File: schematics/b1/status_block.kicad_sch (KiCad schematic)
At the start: 23 parts, among them Q1 2N3904, SW5 SW_SPDT, U4 74HC595

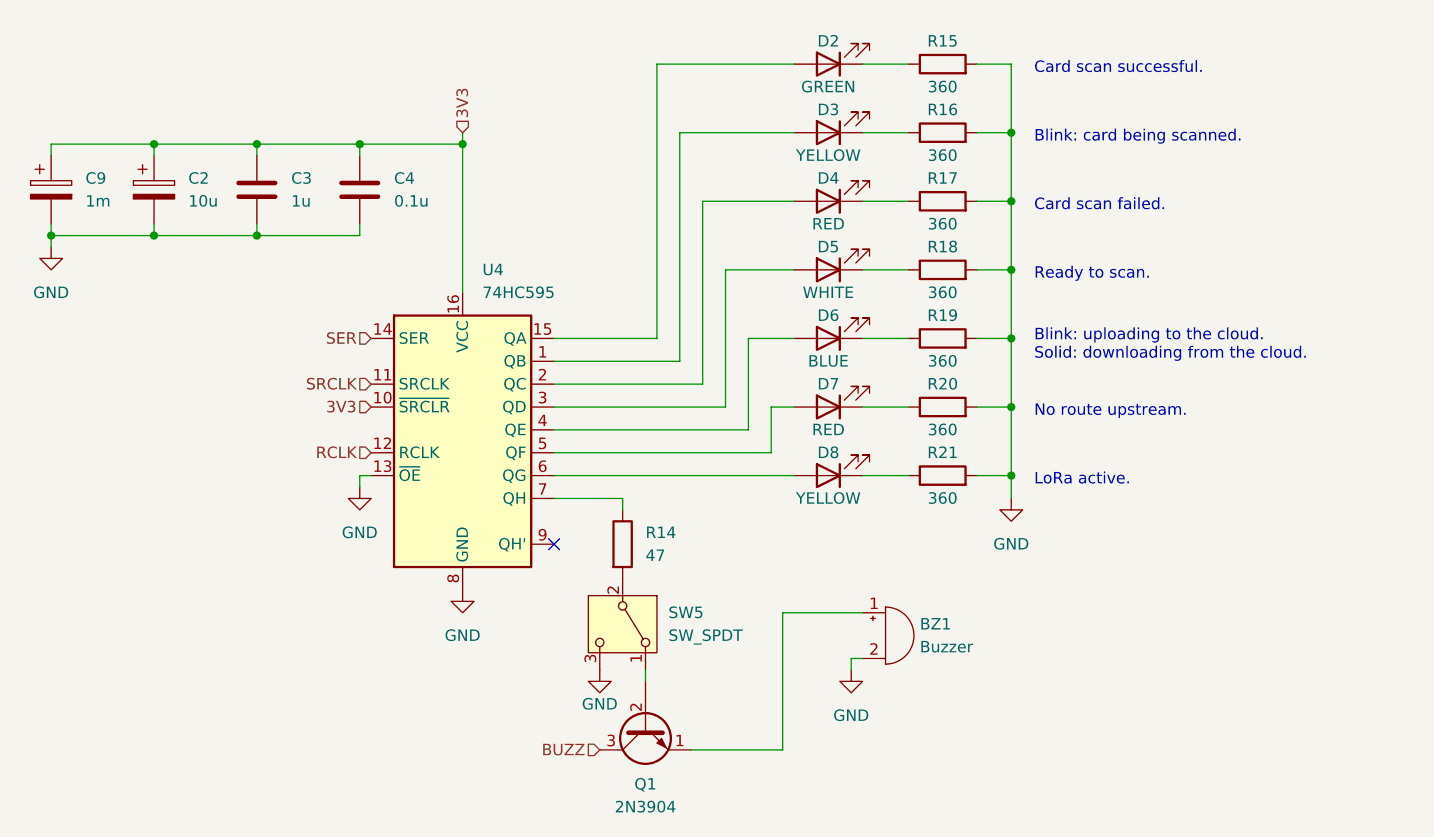
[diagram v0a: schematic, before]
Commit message: Added a bunch of test points.
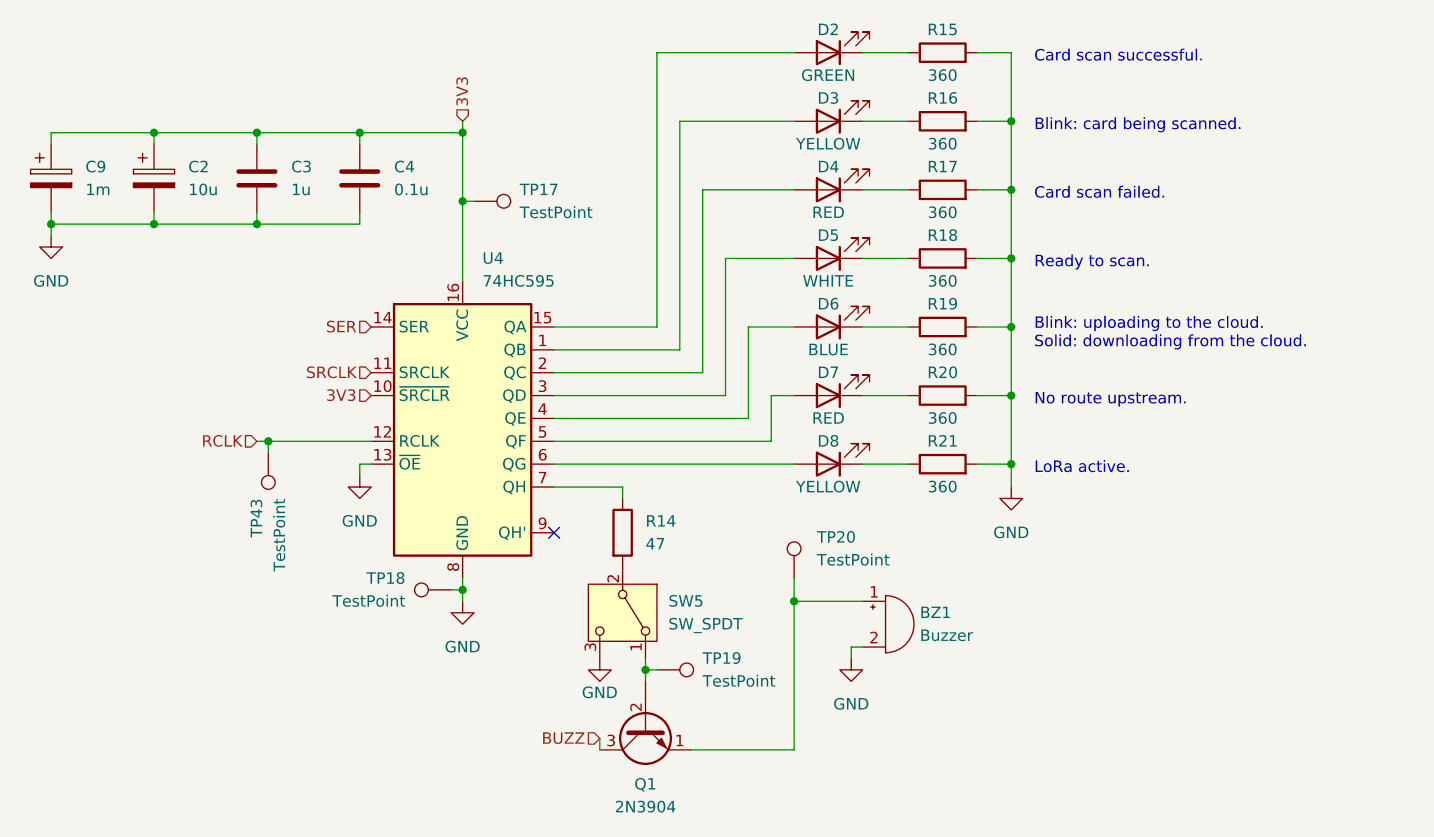
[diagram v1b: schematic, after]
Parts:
- added TP17, TP18, TP19, TP20, TP43: TestPoint, symbol Connector:TestPoint
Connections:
- net 3V3: now also TP17.1
- net GND: now also TP18.1
- net RCLK: now also TP43.1
- net at BZ1.1 (+), Q1.1 (E): now also TP20.1
- net at Q1.2 (B), SW5.1 (A): now also TP19.1
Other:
- moved on the sheet: BZ1, C2, C3, C4, C9, D2, D3, D4, D5, D6, D7, D8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

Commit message: Updated annotations.
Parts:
- renumbered C9 to C21, C2 to C22, C3 to C23, C4 to C24, D2 to D1, D3 to D2, D4 to D3, D5 to D4, D6 to D5, D7 to D6, D8 to D7, R15 to R14, R16 to R15, R17 to R16, R18 to R17, R19 to R18, R20 to R19, R21 to R20, R14 to R21, SW5 to SW6, TP17 to TP32, TP43 to TP33, TP20 to TP34, TP18 to TP35, TP19 to TP36, U4 to U6

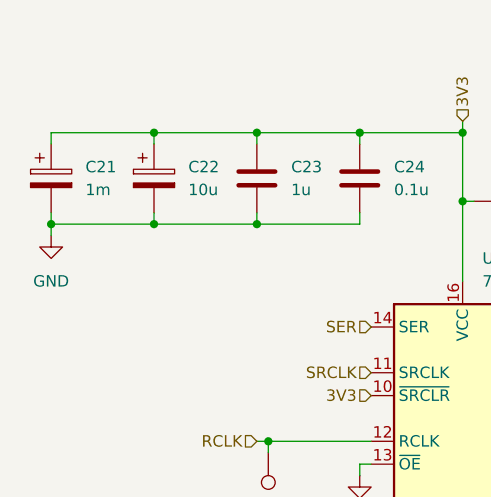
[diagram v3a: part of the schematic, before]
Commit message: Tweaked wiring.
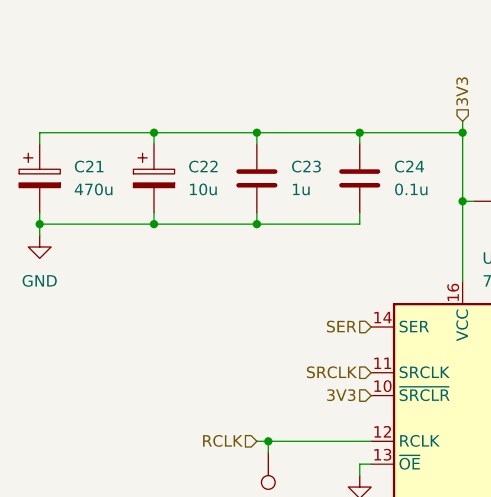
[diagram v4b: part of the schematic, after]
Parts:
- C21: value 1m -> 470u
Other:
- moved on the sheet: C21
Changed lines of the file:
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@@
   (junction (at 45.72 36.83) (diameter 0) (color 0 0 0 0)
   )
-  (junction (at 34.29 36.83) (diameter 0) (color 0 0 0 0)
+  (junction (at 33.02 36.83) (diameter 0) (color 0 0 0 0)
   )
   (junction (at 57.15 26.67) (diameter 0) (color 0 0 0 0)
@@
   )
   (no_connect (at 90.17 71.12))
-  (wire (pts (xy 34.29 27.94) (xy 34.29 26.67))
+  (wire (pts (xy 33.02 27.94) (xy 33.02 26.67))
     (stroke (width 0) (type default))
   )
@@
     (stroke (width 0) (type default))
   )
-  (wire (pts (xy 34.29 38.1) (xy 34.29 36.83))
+  (wire (pts (xy 33.02 38.1) (xy 33.02 36.83))
     (stroke (width 0) (type default))
   )
@@
     (stroke (width 0) (type default))
   )
-  (wire (pts (xy 34.29 35.56) (xy 34.29 36.83))
+  (wire (pts (xy 33.02 35.56) (xy 33.02 36.83))
     (stroke (width 0) (type default))
   )
@@
     (stroke (width 0) (type default))
   )
-  (wire (pts (xy 34.29 36.83) (xy 45.72 36.83))
+  (wire (pts (xy 33.02 36.83) (xy 45.72 36.83))
     (stroke (width 0) (type default))
   )
@@
     (stroke (width 0) (type default))
   )
-  (wire (pts (xy 34.29 26.67) (xy 45.72 26.67))
+  (wire (pts (xy 33.02 26.67) (xy 45.72 26.67))
     (stroke (width 0) (type default))
   )
@@
     )
   )
-  (symbol (lib_id "power:GND") (at 34.29 38.1 0) (unit 1)
+  (symbol (lib_id "power:GND") (at 33.02 38.1 0) (unit 1)
     (in_bom yes) (on_board yes) (dnp no) (fields_autoplaced)
-    (property "Reference" "#PWR029" (at 34.29 44.45 0)
-      (effects (font (size 1.27 1.27)) hide)
-    )
-    (property "Value" "GND" (at 34.29 43.18 0)
-      (effects (font (size 1.27 1.27)))
-    )
-    (property "Footprint" "" (at 34.29 38.1 0)
-      (effects (font (size 1.27 1.27)) hide)
-    )
-    (property "Datasheet" "" (at 34.29 38.1 0)
+    (property "Reference" "#PWR029" (at 33.02 44.45 0)
+      (effects (font (size 1.27 1.27)) hide)
+    )
+    (property "Value" "GND" (at 33.02 43.18 0)
+      (effects (font (size 1.27 1.27)))
+    )
+    (property "Footprint" "" (at 33.02 38.1 0)
+      (effects (font (size 1.27 1.27)) hide)
+    )
+    (property "Datasheet" "" (at 33.02 38.1 0)
       (effects (font (size 1.27 1.27)) hide)
     )
@@
     )
   )
-  (symbol (lib_id "Device:C_Polarized") (at 34.29 31.75 0) (unit 1)
-    (in_bom yes) (on_board yes) (dnp no)
-    (property "Reference" "C21" (at 38.1 30.48 0)
-      (effects (font (size 1.27 1.27)) (justify left))
-    )
-    (property "Value" "1m" (at 38.1 33.02 0)
-      (effects (font (size 1.27 1.27)) (justify left))
-    )
-    (property "Footprint" "" (at 35.2552 35.56 0)
-      (effects (font (size 1.27 1.27)) hide)
-    )
-    (property "Datasheet" "~" (at 34.29 31.75 0)
-      (effects (font (size 1.27 1.27)) hide)
-    )
+  (symbol (lib_id "Device:C_Polarized") (at 33.02 31.75 0) (unit 1)
+    (in_bom yes) (on_board yes) (dnp no)
+    (property "Reference" "C21" (at 36.83 30.48 0)
+      (effects (font (size 1.27 1.27)) (justify left))
+    )
+    (property "Value" "470u" (at 36.83 33.02 0)
+      (effects (font (size 1.27 1.27)) (justify left))
+    )
+    (property "Footprint" "" (at 33.9852 35.56 0)
+      (effects (font (size 1.27 1.27)) hide)
+    )
+    (property "Datasheet" "~" (at 33.02 31.75 0)
+      (effects (font (size 1.27 1.27)) hide)
+    )

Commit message: Assigned some footprints.
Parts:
- BZ1: footprint (none) -> Buzzer_Beeper:Buzzer_12x9.5RM7.6
- C21: footprint (none) -> Capacitor_THT:CP_Radial_D8.0mm_P3.80mm
- C22: footprint (none) -> Capacitor_THT:CP_Radial_D4.0mm_P2.00mm
- C23, C24: footprint (none) -> Capacitor_SMD:C_1206_3216Metric_Pad1.33x1.80mm_HandSolder
- D1, D2, D3, D4, D5, D6, D7: footprint (none) -> LED_THT:LED_D5.0mm
- Q1: footprint Package_TO_SOT_THT:TO-92_Inline -> (none)
- R14, R15, R16, R17, R18, R19, R20, R21: footprint (none) -> Resistor_THT:R_Axial_DIN0207_L6.3mm_D2.5mm_P7.62mm_Horizontal
- SW6: footprint (none) -> custom:SW_SPDT
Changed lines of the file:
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@@
       (effects (font (size 1.27 1.27)))
     )
-    (property "Footprint" "" (at 133.35 27.178 90)
+    (property "Footprint" "Resistor_THT:R_Axial_DIN0207_L6.3mm_D2.5mm_P7.62mm_Horizontal" (at 133.35 27.178 90)
       (effects (font (size 1.27 1.27)) hide)
     )
@@
       (effects (font (size 1.27 1.27)))
     )
-    (property "Footprint" "" (at 120.65 63.5 0)
+    (property "Footprint" "LED_THT:LED_D5.0mm" (at 120.65 63.5 0)
       (effects (font (size 1.27 1.27)) hide)
     )
@@
       (effects (font (size 1.27 1.27)) (justify left))
     )
-    (property "Footprint" "" (at 58.1152 35.56 0)
+    (property "Footprint" "Capacitor_SMD:C_1206_3216Metric_Pad1.33x1.80mm_HandSolder" (at 58.1152 35.56 0)
       (effects (font (size 1.27 1.27)) hide)
     )
@@
       (effects (font (size 1.27 1.27)))
     )
-    (property "Footprint" "" (at 120.65 48.26 0)
+    (property "Footprint" "LED_THT:LED_D5.0mm" (at 120.65 48.26 0)
       (effects (font (size 1.27 1.27)) hide)
     )
@@
       (effects (font (size 1.27 1.27)))
     )
-    (property "Footprint" "" (at 133.35 19.558 90)
+    (property "Footprint" "Resistor_THT:R_Axial_DIN0207_L6.3mm_D2.5mm_P7.62mm_Horizontal" (at 133.35 19.558 90)
       (effects (font (size 1.27 1.27)) hide)
     )
@@
       (effects (font (size 1.27 1.27)) (justify left))
     )
-    (property "Footprint" "" (at 46.6852 35.56 0)
+    (property "Footprint" "Capacitor_THT:CP_Radial_D4.0mm_P2.00mm" (at 46.6852 35.56 0)
       (effects (font (size 1.27 1.27)) hide)
     )
@@
       (effects (font (size 1.27 1.27)))
     )
-    (property "Footprint" "" (at 133.35 57.658 90)
+    (property "Footprint" "Resistor_THT:R_Axial_DIN0207_L6.3mm_D2.5mm_P7.62mm_Horizontal" (at 133.35 57.658 90)
       (effects (font (size 1.27 1.27)) hide)
     )
@@
       (effects (font (size 1.27 1.27)) (justify left))
     )
-    (property "Footprint" "" (at 33.9852 35.56 0)
+    (property "Footprint" "Capacitor_THT:CP_Radial_D8.0mm_P3.80mm" (at 33.9852 35.56 0)
       (effects (font (size 1.27 1.27)) hide)
     )
@@
       (effects (font (size 1.27 1.27)))
     )
-    (property "Footprint" "" (at 120.65 55.88 0)
+    (property "Footprint" "LED_THT:LED_D5.0mm" (at 120.65 55.88 0)
       (effects (font (size 1.27 1.27)) hide)
     )
@@
       (effects (font (size 1.27 1.27)))
     )
-    (property "Footprint" "Package_TO_SOT_THT:TO-92_Inline" (at 102.235 97.79 0)
+    (property "Footprint" "" (at 102.235 97.79 0)
       (effects (font (size 1.27 1.27) italic) (justify left) hide)
     )
@@
       (effects (font (size 1.27 1.27)))
     )
-    (property "Footprint" "" (at 120.65 25.4 0)
+    (property "Footprint" "LED_THT:LED_D5.0mm" (at 120.65 25.4 0)
       (effects (font (size 1.27 1.27)) hide)
     )
@@
       (effects (font (size 1.27 1.27)))
     )
-    (property "Footprint" "" (at 120.65 17.78 0)
+    (property "Footprint" "LED_THT:LED_D5.0mm" (at 120.65 17.78 0)
       (effects (font (size 1.27 1.27)) hide)
     )
@@
       (effects (font (size 1.27 1.27)))
     )
-    (property "Footprint" "" (at 133.35 34.798 90)
+    (property "Footprint" "Resistor_THT:R_Axial_DIN0207_L6.3mm_D2.5mm_P7.62mm_Horizontal" (at 133.35 34.798 90)
       (effects (font (size 1.27 1.27)) hide)
     )
@@
       (effects (font (size 1.27 1.27)))
     )
-    (property "Footprint" "" (at 120.65 40.64 0)
+    (property "Footprint" "LED_THT:LED_D5.0mm" (at 120.65 40.64 0)
       (effects (font (size 1.27 1.27)) hide)
     )
@@
       (effects (font (size 1.27 1.27)) (justify left))
     )
-    (property "Footprint" "" (at 126.365 78.74 90)
+    (property "Footprint" "Buzzer_Beeper:Buzzer_12x9.5RM7.6" (at 126.365 78.74 90)
       (effects (font (size 1.27 1.27)) hide)
     )
@@
       (effects (font (size 1.27 1.27)) (justify left))
     )
-    (property "Footprint" "" (at 69.5452 35.56 0)
+    (property "Footprint" "Capacitor_SMD:C_1206_3216Metric_Pad1.33x1.80mm_HandSolder" (at 69.5452 35.56 0)
       (effects (font (size 1.27 1.27)) hide)
     )
@@
       (effects (font (size 1.27 1.27)))
     )
-    (property "Footprint" "" (at 133.35 65.278 90)
+    (property "Footprint" "Resistor_THT:R_Axial_DIN0207_L6.3mm_D2.5mm_P7.62mm_Horizontal" (at 133.35 65.278 90)
       (effects (font (size 1.27 1.27)) hide)
     )
@@
       (effects (font (size 1.27 1.27)))
     )
-    (property "Footprint" "" (at 120.65 33.02 0)
+    (property "Footprint" "LED_THT:LED_D5.0mm" (at 120.65 33.02 0)
       (effects (font (size 1.27 1.27)) hide)
     )
@@
       (effects (font (size 1.27 1.27)))
     )
-    (property "Footprint" "" (at 133.35 50.038 90)
+    (property "Footprint" "Resistor_THT:R_Axial_DIN0207_L6.3mm_D2.5mm_P7.62mm_Horizontal" (at 133.35 50.038 90)
       (effects (font (size 1.27 1.27)) hide)
     )
@@
       (effects (font (size 1.27 1.27)) (justify left))
     )
-    (property "Footprint" "" (at 96.012 71.12 90)
+    (property "Footprint" "Resistor_THT:R_Axial_DIN0207_L6.3mm_D2.5mm_P7.62mm_Horizontal" (at 96.012 71.12 90)
       (effects (font (size 1.27 1.27)) hide)
     )
@@
       (effects (font (size 1.27 1.27)) (justify left))
     )
-    (property "Footprint" "" (at 97.79 80.01 0)
+    (property "Footprint" "custom:SW_SPDT" (at 97.79 80.01 0)
       (effects (font (size 1.27 1.27)) hide)
     )
@@
       (effects (font (size 1.27 1.27)))
     )
-    (property "Footprint" "" (at 133.35 42.418 90)
-      (effects (font (size 1.27 1.27)) hide)
-    )
+    (property "Footprint" "Resistor_THT:R_Axial_DIN0207_L6.3mm_D2.5mm_P7.62mm_Horizontal" (at 133.35 42.418 90)
+      (effects (font (size 1.27 1.27)) hide)
+    )

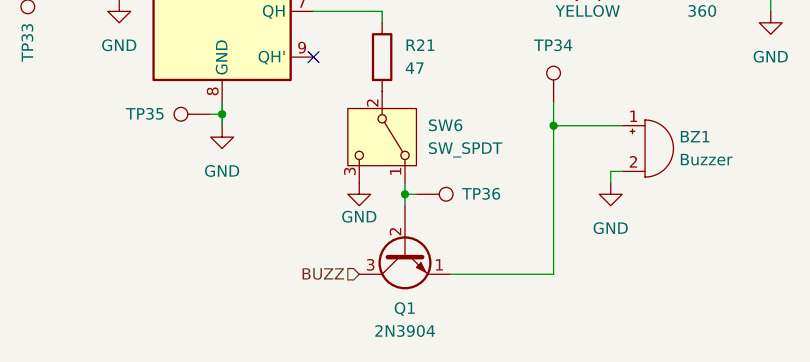
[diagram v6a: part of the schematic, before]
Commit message: Finished assigning footprints.
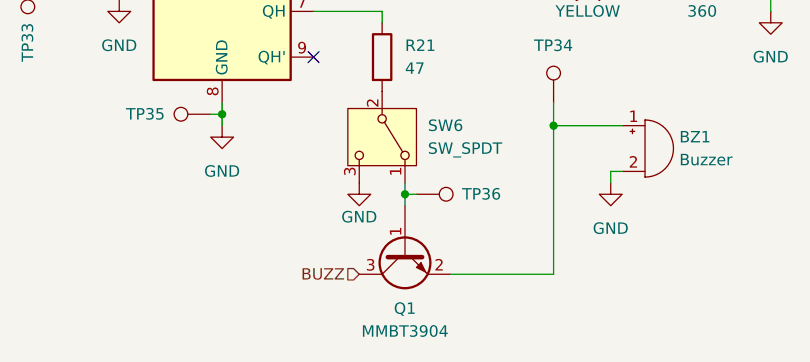
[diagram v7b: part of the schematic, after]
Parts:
- Q1: value 2N3904 -> MMBT3904; footprint (none) -> Package_TO_SOT_SMD:SOT-23; symbol Transistor_BJT:2N3904 -> Transistor_BJT:MMBT3904
- TP32, TP33, TP34, TP35, TP36: footprint (none) -> TestPoint:TestPoint_Loop_D2.50mm_Drill1.0mm
- U6: footprint (none) -> SN74HC595N:DIP794W45P254L1969H508Q16
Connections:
- net at BZ1.1 (+), TP34.1: now also Q1.2 (E); no longer Q1.1 (E)
- net at SW6.1 (A), TP36.1: now also Q1.1 (B); no longer Q1.2 (B)
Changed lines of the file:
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@@
       (effects (font (size 1.27 1.27)) (justify left) hide)
     )
-    (property "Footprint" "" (at 53.34 62.23 0)
+    (property "Footprint" "TestPoint:TestPoint_Loop_D2.50mm_Drill1.0mm" (at 53.34 62.23 0)
       (effects (font (size 1.27 1.27)) hide)
     )
@@
       (effects (font (size 1.27 1.27)) (justify left) hide)
     )
-    (property "Footprint" "" (at 81.28 39.37 0)
+    (property "Footprint" "TestPoint:TestPoint_Loop_D2.50mm_Drill1.0mm" (at 81.28 39.37 0)
       (effects (font (size 1.27 1.27)) hide)
     )
@@
       (effects (font (size 1.27 1.27)) (justify left) hide)
     )
-    (property "Footprint" "" (at 121.92 76.2 0)
+    (property "Footprint" "TestPoint:TestPoint_Loop_D2.50mm_Drill1.0mm" (at 121.92 76.2 0)
       (effects (font (size 1.27 1.27)) hide)
     )
@@
       (effects (font (size 1.27 1.27)) (justify left))
     )
-    (property "Footprint" "" (at 80.01 58.42 0)
+    (property "Footprint" "SN74HC595N:DIP794W45P254L1969H508Q16" (at 80.01 58.42 0)
       (effects (font (size 1.27 1.27)) hide)
     )
@@
     )
   )
-  (symbol (lib_id "Transistor_BJT:2N3904") (at 100.33 92.71 90) (mirror x) (unit 1)
+  (symbol (lib_id "Transistor_BJT:MMBT3904") (at 100.33 92.71 90) (mirror x) (unit 1)
     (in_bom yes) (on_board yes) (dnp no)
     (property "Reference" "Q1" (at 100.33 99.06 90)
       (effects (font (size 1.27 1.27)))
     )
-    (property "Value" "2N3904" (at 100.33 101.6 90)
-      (effects (font (size 1.27 1.27)))
-    )
-    (property "Footprint" "" (at 102.235 97.79 0)
+    (property "Value" "MMBT3904" (at 100.33 101.6 90)
+      (effects (font (size 1.27 1.27)))
+    )
+    (property "Footprint" "Package_TO_SOT_SMD:SOT-23" (at 102.235 97.79 0)
       (effects (font (size 1.27 1.27) italic) (justify left) hide)
     )
-    (property "Datasheet" "https://www.onsemi.com/pub/Collateral/2N3903-D.PDF" (at 100.33 92.71 0)
+    (property "Datasheet" "https://www.onsemi.com/pdf/datasheet/pzt3904-d.pdf" (at 100.33 92.71 0)
       (effects (font (size 1.27 1.27)) (justify left) hide)
     )
@@
       (effects (font (size 1.27 1.27)) (justify left) hide)
     )
-    (property "Footprint" "" (at 101.6 91.44 0)
+    (property "Footprint" "TestPoint:TestPoint_Loop_D2.50mm_Drill1.0mm" (at 101.6 91.44 0)
       (effects (font (size 1.27 1.27)) hide)
     )
@@
       (effects (font (size 1.27 1.27)) (justify left) hide)
     )
-    (property "Footprint" "" (at 78.74 72.39 0)
-      (effects (font (size 1.27 1.27)) hide)
-    )
+    (property "Footprint" "TestPoint:TestPoint_Loop_D2.50mm_Drill1.0mm" (at 78.74 72.39 0)
+      (effects (font (size 1.27 1.27)) hide)
+    )

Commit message: Routed traces.
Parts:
- D1: value GREEN -> WHITE
- D3: value RED -> GREEN
- D4: value WHITE -> RED
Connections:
- net at D7.2 (A): now also U6.7 (QH); no longer U6.6 (QG)
- net at D5.2 (A): now also U6.5 (QF); no longer U6.4 (QE)
- net at U6.1 (QB): now also D1.2 (A); no longer D2.2 (A)
- net at U6.15 (QA): now also R21.1; no longer D1.2 (A)
- net at U6.2 (QC): now also D2.2 (A); no longer D3.2 (A)
- net at U6.3 (QD): now also D3.2 (A); no longer D4.2 (A)
- net at D6.2 (A): now also U6.6 (QG); no longer U6.5 (QF)
- new net: D4.2 (A), U6.4 (QE)
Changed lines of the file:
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@@
     (effects (font (size 1.27 1.27)) (justify left bottom))
   )
-  (text "Card scan successful." (at 143.51 19.05 0)
+  (text "Card scan successful." (at 143.51 34.29 0)
     (effects (font (size 1.27 1.27)) (justify left bottom))
   )
@@
     (effects (font (size 1.27 1.27)) (justify left bottom))
   )
-  (text "Card scan failed." (at 143.51 34.29 0)
+  (text "Card scan failed." (at 143.51 41.91 0)
     (effects (font (size 1.27 1.27)) (justify left bottom))
   )
-  (text "Ready to scan." (at 143.51 41.91 0)
+  (text "Ready to scan." (at 143.51 19.05 0)
     (effects (font (size 1.27 1.27)) (justify left bottom))
   )
@@
       (effects (font (size 1.27 1.27)))
     )
-    (property "Value" "GREEN" (at 120.65 20.32 0)
+    (property "Value" "WHITE" (at 120.65 20.32 0)
       (effects (font (size 1.27 1.27)))
     )
@@
       (effects (font (size 1.27 1.27)))
     )
-    (property "Value" "WHITE" (at 120.65 43.18 0)
+    (property "Value" "RED" (at 120.65 43.18 0)
       (effects (font (size 1.27 1.27)))
     )
@@
       (effects (font (size 1.27 1.27)))
     )
-    (property "Value" "RED" (at 120.65 35.56 0)
-      (effects (font (size 1.27 1.27)))
-    )
+    (property "Value" "GREEN" (at 120.65 35.56 0)
+      (effects (font (size 1.27 1.27)))
+    )
